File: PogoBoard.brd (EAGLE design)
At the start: 29.7 x 30 mm, 4 parts

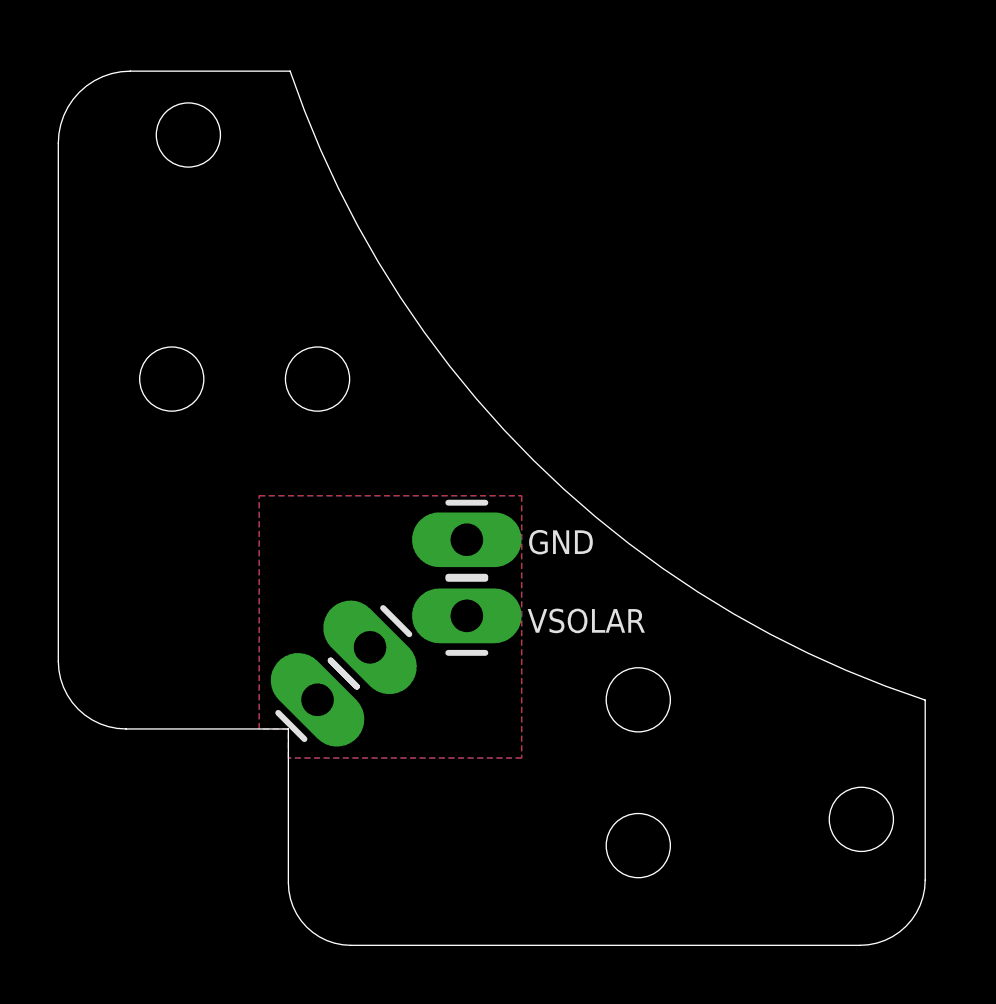
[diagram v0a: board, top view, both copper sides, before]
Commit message: Changed pogo board screws to M3
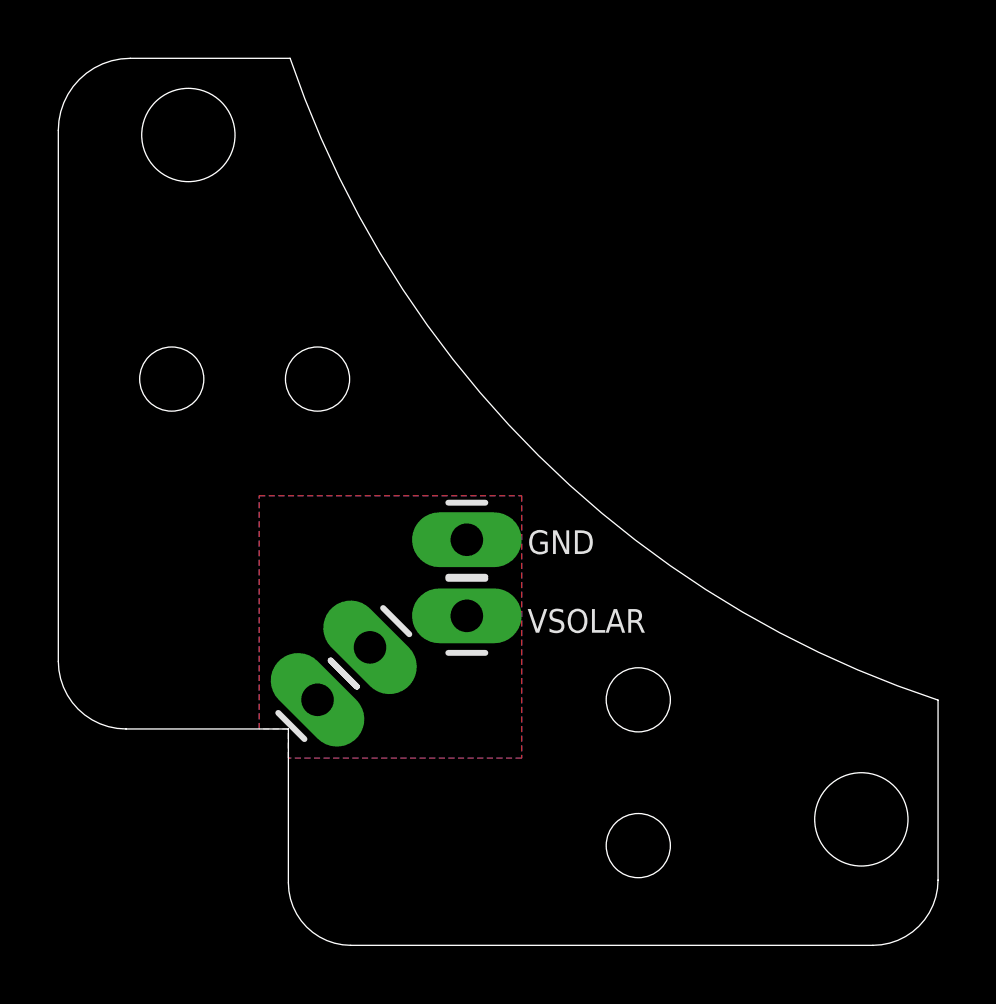
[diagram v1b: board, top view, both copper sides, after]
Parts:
- added FRAME1: FRAME-LETTER, SparkFun-Aesthetics:CREATIVE_COMMONS
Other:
- board size 29.7 x 30 mm -> 30.2 x 30.4 mm
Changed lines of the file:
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@@
 <layer number="106" name="bPlate" color="7" fill="1" visible="yes" active="yes"/>
 <layer number="107" name="Crop" color="7" fill="1" visible="yes" active="yes"/>
+<layer number="108" name="tplace-old" color="10" fill="1" visible="no" active="yes"/>
+<layer number="109" name="ref-old" color="11" fill="1" visible="no" active="yes"/>
 <layer number="116" name="Patch_BOT" color="9" fill="4" visible="yes" active="yes"/>
 <layer number="121" name="_tsilk" color="7" fill="1" visible="yes" active="yes"/>
 <layer number="122" name="_bsilk" color="7" fill="1" visible="yes" active="yes"/>
+<layer number="125" name="_tNames" color="7" fill="1" visible="yes" active="yes"/>
 <layer number="144" name="Drill_legend" color="7" fill="1" visible="yes" active="yes"/>
 <layer number="151" name="HeatSink" color="7" fill="1" visible="yes" active="yes"/>
+<layer number="199" name="Contour" color="7" fill="1" visible="yes" active="yes"/>
 <layer number="200" name="200bmp" color="1" fill="10" visible="yes" active="yes"/>
 <layer number="201" name="201bmp" color="2" fill="10" visible="yes" active="yes"/>
@@
 <layer number="215" name="215bmp" color="7" fill="1" visible="yes" active="yes"/>
 <layer number="216" name="216bmp" color="7" fill="1" visible="yes" active="yes"/>
+<layer number="217" name="217bmp" color="18" fill="1" visible="no" active="no"/>
+<layer number="218" name="218bmp" color="19" fill="1" visible="no" active="no"/>
+<layer number="219" name="219bmp" color="20" fill="1" visible="no" active="no"/>
+<layer number="220" name="220bmp" color="21" fill="1" visible="no" active="no"/>
+<layer number="221" name="221bmp" color="22" fill="1" visible="no" active="no"/>
+<layer number="222" name="222bmp" color="23" fill="1" visible="no" active="no"/>
+<layer number="223" name="223bmp" color="24" fill="1" visible="no" active="no"/>
+<layer number="224" name="224bmp" color="25" fill="1" visible="no" active="no"/>
 <layer number="250" name="Descript" color="3" fill="1" visible="no" active="no"/>
 <layer number="251" name="SMDround" color="12" fill="11" visible="no" active="no"/>
@@
 <wire x1="0" y1="0" x2="-5.56834375" y2="0" width="0" layer="20"/>
 <wire x1="-5.56834375" y1="0" x2="-7.89" y2="2.32165625" width="0" layer="20" curve="-90"/>
-<wire x1="-7.89" y1="2.32165625" x2="-7.89" y2="20.091865625" width="0" layer="20"/>
-<wire x1="-7.89" y1="20.091865625" x2="-5.421865625" y2="22.56" width="0" layer="20" curve="-90"/>
-<wire x1="-5.421865625" y1="22.56" x2="0.06" y2="22.56" width="0" layer="20"/>
+<wire x1="-7.89" y1="2.32165625" x2="-7.89" y2="20.531865625" width="0" layer="20"/>
+<wire x1="-7.89" y1="20.531865625" x2="-5.421865625" y2="23" width="0" layer="20" curve="-90"/>
+<wire x1="-5.421865625" y1="23" x2="0.06" y2="23" width="0" layer="20"/>
 <wire x1="0" y1="0" x2="0" y2="-5.27888125" width="0" layer="20"/>
 <wire x1="0" y1="-5.27888125" x2="2.14111875" y2="-7.42" width="0" layer="20" curve="90"/>
-<wire x1="2.14111875" y1="-7.42" x2="19.603934375" y2="-7.42" width="0" layer="20"/>
-<wire x1="19.603934375" y1="-7.42" x2="21.84" y2="-5.183934375" width="0" layer="20" curve="90"/>
-<wire x1="21.84" y1="-5.183934375" x2="21.84" y2="0.99" width="0" layer="20"/>
-<wire x1="21.84" y1="0.99" x2="0.06" y2="22.56" width="0" layer="20" curve="-53.015"/>
-<hole x="-3.43" y="20.37" drill="2.2"/>
-<hole x="19.65" y="-3.1" drill="2.2"/>
+<wire x1="2.14111875" y1="-7.42" x2="20.043934375" y2="-7.42" width="0" layer="20"/>
+<wire x1="20.043934375" y1="-7.42" x2="22.28" y2="-5.183934375" width="0" layer="20" curve="90"/>
+<wire x1="22.28" y1="-5.183934375" x2="22.28" y2="0.99" width="0" layer="20"/>
+<wire x1="22.28" y1="0.99" x2="0.06" y2="23" width="0" layer="20" curve="-53.015"/>
+<hole x="-3.43" y="20.37" drill="3.2"/>
+<hole x="19.65" y="-3.1" drill="3.2"/>
 <text x="8.2" y="3.3" size="0.8128" layer="21">VSOLAR</text>
 <text x="8.2" y="6" size="0.8128" layer="21">GND</text>
@@
 <element name="JP3" library="SparkFun" package="1X01_LONGPAD" value="M01PTH_LONGPAD" x="2.8" y="2.8" smashed="yes" rot="R225"/>
 <element name="JP4" library="SparkFun" package="1X01_LONGPAD" value="M01PTH_LONGPAD" x="1" y="1" smashed="yes" rot="R225"/>
+<element name="FRAME1" library="SparkFun-Aesthetics" package="CREATIVE_COMMONS" value="FRAME-LETTER" x="3.4" y="-21"/>
 </elements>
 <signals>
